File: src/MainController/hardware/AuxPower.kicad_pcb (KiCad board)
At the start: 2 copper layers, 90 x 90 mm, 123 parts, among them J1 MC 1,5/2, J10 MC 1,5/4, J11 S3B-XH-A, J12 S3B-XH-A, J13 S3B-XH-A, J14 S3B-XH-A, J15 S3B-XH-A, J16 B3B-XH-A, J17 B4B-XH-A, J2 MC 1,5/2, J3 MC 1,5/2, J4 MC 1,5/2, J5 MC 1,5/2, J6 MC 1,5/4, J7 MC 1,5/4, J8 MC 1,5/4, J9 MC 1,5/4, Q1 BC846B,235, Q10 AO4421, Q2 BC846B,235, Q3 BC846B,235, Q4 BC846B,235, Q5 BC846B,235, Q6 AO4421, Q7 AO4421, Q8 AO4421, Q9 AO4421, U1 ZXCT1009, U2 ZXCT1009, U3 ZXCT1009, U5 ZXCT1009, U6 PIC18F26K83, U7 PI4IOE5V6416, U8 MCP9701

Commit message: MainController: adjusting voltage dividers
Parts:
- R36: renamed from R37; value 6K2 -> 4K42
- R37: renamed from R38; value 6K2 -> 4K42
- R38: renamed from R39; value 6K2 -> 4K42
- R39: renamed from R40; value 6K2 -> 4K42
- R40: renamed from R41; value 6K2 -> 4K42
- R41: renamed from R29; value 3K -> 5K6
- R57: value 18K -> 39K2
- R58, R59, R60, R61, R62: value 180K -> 137K
- renumbered R30 to R29, R31 to R30, R32 to R31, R33 to R32, R34 to R33, R35 to R34, R36 to R35
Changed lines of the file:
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@@
 		(at 34.8 51 90)
 		(tags "RESC2013X70N")
-		(property "Reference" "R39"
+		(property "Reference" "R38"
 			(at 0 1.6 90)
 			(layer "B.SilkS")
@@
 			)
 		)
-		(property "Value" "6K2"
+		(property "Value" "4K42"
 			(at 2.3 0 0)
 			(layer "B.SilkS")
@@
 			)
 		)
-		(property "Value" "180K"
+		(property "Value" "137K"
 			(at 2.3 0 0)
 			(layer "B.SilkS")
@@
 			)
 		)
-		(property "Value" "180K"
+		(property "Value" "137K"
 			(at 2.3 0 0)
 			(layer "B.SilkS")
@@
 			)
 		)
-		(property "Value" "180K"
+		(property "Value" "137K"
 			(at 2.3 0 0)
 			(layer "B.SilkS")
@@
 		(at 44.4 51 90)
 		(tags "RESC2013X70N")
-		(property "Reference" "R40"
+		(property "Reference" "R39"
 			(at 0 1.6 90)
 			(layer "B.SilkS")
@@
 			)
 		)
-		(property "Value" "6K2"
+		(property "Value" "4K42"
 			(at 2.3 0 0)
 			(layer "B.SilkS")
@@
 		(at 20.5 92 90)
 		(tags "RESC2013X70N")
-		(property "Reference" "R30"
+		(property "Reference" "R29"
 			(at 0 1.6 90)
 			(layer "B.SilkS")
@@
 		(at 38.7 84.15)
 		(tags "RESC2013X70N")
-		(property "Reference" "R36"
+		(property "Reference" "R35"
 			(at 0 1.6 0)
 			(layer "B.SilkS")
@@
 		(at 34.3 84.25 180)
 		(tags "RESC2013X70N")
-		(property "Reference" "R35"
+		(property "Reference" "R34"
 			(at 0 1.6 0)
 			(layer "B.SilkS")
@@
 		(at 54 51 90)
 		(tags "RESC2013X70N")
-		(property "Reference" "R41"
+		(property "Reference" "R40"
 			(at 0 1.6 90)
 			(layer "B.SilkS")
@@
 			)
 		)
-		(property "Value" "6K2"
+		(property "Value" "4K42"
 			(at 2.3 0 0)
 			(layer "B.SilkS")
@@
 		(at 52 92 90)
 		(tags "RESC2013X70N")
-		(property "Reference" "R33"
+		(property "Reference" "R32"
 			(at 0 1.6 90)
 			(layer "B.SilkS")
@@
 		(at 31 92 90)
 		(tags "RESC2013X70N")
-		(property "Reference" "R31"
+		(property "Reference" "R30"
 			(at 0 1.6 90)
 			(layer "B.SilkS")
@@
 		(at 22.8 45 90)
 		(tags "RESC2013X70N")
-		(property "Reference" "R37"
+		(property "Reference" "R36"
 			(at 0 1.6 90)
 			(layer "B.SilkS")
@@
 			)
 		)
-		(property "Value" "6K2"
+		(property "Value" "4K42"
 			(at 2.3 0 0)
 			(layer "B.SilkS")
@@
 			)
 		)
-		(property "Value" "180K"
+		(property "Value" "137K"
 			(at 2.3 0 0)
 			(layer "B.SilkS")
@@
 			)
 		)
-		(property "Value" "18K"
+		(property "Value" "39K2"
 			(at 2.3 0 90)
 			(layer "B.SilkS")
@@
 			)
 		)
-		(property "Value" "180K"
+		(property "Value" "137K"
 			(at 2.3 0 0)
 			(layer "B.SilkS")
@@
 		(at 41.5 92 90)
 		(tags "RESC2013X70N")
-		(property "Reference" "R32"
+		(property "Reference" "R31"
 			(at 0 1.6 90)
 			(layer "B.SilkS")
@@
 		(at 62 84.5 180)
 		(tags "RESC2013X70N")
-		(property "Reference" "R29"
+		(property "Reference" "R41"
 			(at 0 1.6 0)
 			(layer "B.SilkS")
@@
 			)
 		)
-		(property "Value" "3K"
+		(property "Value" "5K6"
 			(at 2.3 0 90)
 			(layer "B.SilkS")
@@
 		(at 62.5 92 90)
 		(tags "RESC2013X70N")
-		(property "Reference" "R34"
+		(property "Reference" "R33"
 			(at 0 1.6 90)
 			(layer "B.SilkS")
@@
 		(at 25.2 51 90)
 		(tags "RESC2013X70N")
-		(property "Reference" "R38"
+		(property "Reference" "R37"
 			(at 0 1.6 90)
 			(layer "B.SilkS")
@@
 			)
 		)
-		(property "Value" "6K2"
+		(property "Value" "4K42"
 			(at 2.3 0 0)
 			(layer "B.SilkS")

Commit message: MainController: Replaced main mosfet
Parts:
- Q10, Q6, Q7, Q8, Q9: value AO4421 -> RS3L110
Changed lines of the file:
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@@
 			)
 		)
-		(property "Value" "AO4421"
+		(property "Value" "RS3L110"
 			(at 0.7 0 0)
 			(layer "B.SilkS")
@@
 			)
 		)
-		(property "Value" "AO4421"
+		(property "Value" "RS3L110"
 			(at 0.7 0 0)
 			(layer "B.SilkS")
@@
 			)
 		)
-		(property "Value" "AO4421"
+		(property "Value" "RS3L110"
 			(at 0.7 0 0)
 			(layer "B.SilkS")
@@
 			)
 		)
-		(property "Value" "AO4421"
+		(property "Value" "RS3L110"
 			(at 0.7 0 0)
 			(layer "B.SilkS")
@@
 			)
 		)
-		(property "Value" "AO4421"
+		(property "Value" "RS3L110"
 			(at 0.7 0 0)
 			(layer "B.SilkS")

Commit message: MainController: Adjusted resistor values for MOSFET drive
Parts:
- R47: renamed from R48; value 10K -> 30K
- R48: renamed from R53; value 18K -> 30K
- R49: renamed from R54; value 18K -> 30K
- R50: renamed from R55; value 18K -> 30K
- R51: renamed from R56; value 18K -> 30K
- R53: renamed from R47; value 10K -> 62K
- R54: renamed from R49; value 10K -> 62K
- R55: renamed from R50; value 10K -> 62K
- R56: renamed from R51; value 10K -> 62K
- R57: renamed from R52; value 10K -> 62K
- renumbered R57 to R52
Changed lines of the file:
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@@
 		(at 70 29.5 180)
 		(tags "RESC2013X70N")
-		(property "Reference" "R51"
+		(property "Reference" "R56"
 			(at 0 1.6 0)
 			(layer "B.SilkS")
@@
 			)
 		)
-		(property "Value" "10K"
+		(property "Value" "62K"
 			(at 2.8 0 0)
 			(layer "B.SilkS")
@@
 		(at 19 29.5 180)
 		(tags "RESC2013X70N")
-		(property "Reference" "R47"
+		(property "Reference" "R53"
 			(at 0 1.6 0)
 			(layer "B.SilkS")
@@
 			)
 		)
-		(property "Value" "10K"
+		(property "Value" "62K"
 			(at 2.7 0 0)
 			(layer "B.SilkS")
@@
 		(at 36 31.7 180)
 		(tags "RESC2013X70N")
-		(property "Reference" "R53"
+		(property "Reference" "R48"
 			(at 0 1.6 0)
 			(layer "B.SilkS")
@@
 			)
 		)
-		(property "Value" "18K"
+		(property "Value" "30K"
 			(at 2.8 0 0)
 			(layer "B.SilkS")
@@
 		(at 70 31.7 180)
 		(tags "RESC2013X70N")
-		(property "Reference" "R55"
+		(property "Reference" "R50"
 			(at 0 1.6 0)
 			(layer "B.SilkS")
@@
 			)
 		)
-		(property "Value" "18K"
+		(property "Value" "30K"
 			(at 2.8 0 0)
 			(layer "B.SilkS")
@@
 		(at 87 31.7 180)
 		(tags "RESC2013X70N")
-		(property "Reference" "R56"
+		(property "Reference" "R51"
 			(at 0 1.6 0)
 			(layer "B.SilkS")
@@
 			)
 		)
-		(property "Value" "18K"
+		(property "Value" "30K"
 			(at 2.8 0 0)
 			(layer "B.SilkS")
@@
 		(at 36 29.5 180)
 		(tags "RESC2013X70N")
-		(property "Reference" "R49"
+		(property "Reference" "R54"
 			(at 0 1.6 0)
 			(layer "B.SilkS")
@@
 			)
 		)
-		(property "Value" "10K"
+		(property "Value" "62K"
 			(at 2.8 0 0)
 			(layer "B.SilkS")
@@
 		(at 53 31.7 180)
 		(tags "RESC2013X70N")
-		(property "Reference" "R54"
+		(property "Reference" "R49"
 			(at 0 1.6 0)
 			(layer "B.SilkS")
@@
 			)
 		)
-		(property "Value" "18K"
+		(property "Value" "30K"
 			(at 2.8 0 0)
 			(layer "B.SilkS")
@@
 		(at 19 31.7 180)
 		(tags "RESC2013X70N")
-		(property "Reference" "R48"
+		(property "Reference" "R47"
 			(at 0 1.6 0)
 			(layer "B.SilkS")
@@
 			)
 		)
-		(property "Value" "10K"
+		(property "Value" "30K"
 			(at 2.7 0 0)
 			(layer "B.SilkS")
@@
 		(at 53 29.5 180)
 		(tags "RESC2013X70N")
-		(property "Reference" "R50"
+		(property "Reference" "R55"
 			(at 0 1.6 0)
 			(layer "B.SilkS")
@@
 			)
 		)
-		(property "Value" "10K"
+		(property "Value" "62K"
 			(at 2.8 0 0)
 			(layer "B.SilkS")
@@
 		(at 62 82.1 180)
 		(tags "RESC2013X70N")
-		(property "Reference" "R57"
+		(property "Reference" "R52"
 			(at 0 1.6 0)
 			(layer "B.SilkS")
@@
 		(at 87 29.5 180)
 		(tags "RESC2013X70N")
-		(property "Reference" "R52"
+		(property "Reference" "R57"
 			(at 0 1.6 0)
 			(layer "B.SilkS")
@@
 			)
 		)
-		(property "Value" "10K"
+		(property "Value" "62K"
 			(at 2.8 0 0)
 			(layer "B.SilkS")

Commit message: MainController: Reducing internal LED brightness
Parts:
- R22, R23, R24, R25, R26, R27: value 1K -> 3K3
- R28: renamed from R21; value 1K -> 3K3
- renumbered R28 to R21
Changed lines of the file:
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@@
 		(at 23 92 90)
 		(tags "RESC2013X70N")
-		(property "Reference" "R21"
+		(property "Reference" "R28"
 			(at 0 1.6 90)
 			(layer "B.SilkS")
@@
 			)
 		)
-		(property "Value" "1K"
+		(property "Value" "3K3"
 			(at 2.3 0 0)
 			(layer "B.SilkS")
@@
 		(at 40.5 66.5 180)
 		(tags "RESC2013X70N")
-		(property "Reference" "R28"
+		(property "Reference" "R21"
 			(at 0 1.6 0)
 			(layer "B.SilkS")
@@
 			)
 		)
-		(property "Value" "1K"
+		(property "Value" "3K3"
 			(at 2.3 0 0)
 			(layer "B.SilkS")
@@
 			)
 		)
-		(property "Value" "1K"
+		(property "Value" "3K3"
 			(at 2.3 0 0)
 			(layer "B.SilkS")
@@
 			)
 		)
-		(property "Value" "1K"
+		(property "Value" "3K3"
 			(at 2.3 0 0)
 			(layer "B.SilkS")
@@
 			)
 		)
-		(property "Value" "1K"
+		(property "Value" "3K3"
 			(at 0 1.7 0)
 			(layer "B.SilkS")
@@
 			)
 		)
-		(property "Value" "1K"
+		(property "Value" "3K3"
 			(at -2.35 -0.05 0)
 			(layer "B.SilkS")
@@
 			)
 		)
-		(property "Value" "1K"
+		(property "Value" "3K3"
 			(at 2.3 0 0)
 			(layer "B.SilkS")

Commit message: MainController: Reducing brightness for output LEDs
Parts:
- R17: renamed from R16; value 1K -> 3K3
- R18: renamed from R17; value 1K -> 3K3
- R19: renamed from R18; value 1K -> 3K3
- R20: renamed from R19; value 1K -> 3K3
- R21: renamed from R20; value 1K -> 3K3
- renumbered R21 to R16
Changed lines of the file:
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@@
 		(at 48.1 65 -90)
 		(tags "RESC2013X70N")
-		(property "Reference" "R20"
+		(property "Reference" "R21"
 			(at 0 1.6 90)
 			(layer "B.SilkS")
@@
 			)
 		)
-		(property "Value" "1K"
+		(property "Value" "3K3"
 			(at -2.3 0 0)
 			(layer "B.SilkS")
@@
 		(at 42.6 59.7 -90)
 		(tags "RESC2013X70N")
-		(property "Reference" "R16"
+		(property "Reference" "R17"
 			(at 0 1.6 90)
 			(layer "B.SilkS")
@@
 			)
 		)
-		(property "Value" "1K"
+		(property "Value" "3K3"
 			(at -2.3 0.3 0)
 			(layer "B.SilkS")
@@
 		(at 49.2 59.7 -90)
 		(tags "RESC2013X70N")
-		(property "Reference" "R19"
+		(property "Reference" "R20"
 			(at 0 1.6 90)
 			(layer "B.SilkS")
@@
 			)
 		)
-		(property "Value" "1K"
+		(property "Value" "3K3"
 			(at -2.3 -0.25 0)
 			(layer "B.SilkS")
@@
 		(at 40.5 66.5 180)
 		(tags "RESC2013X70N")
-		(property "Reference" "R21"
+		(property "Reference" "R16"
 			(at 0 1.6 0)
 			(layer "B.SilkS")
@@
 		(at 44.8 59.7 -90)
 		(tags "RESC2013X70N")
-		(property "Reference" "R17"
+		(property "Reference" "R18"
 			(at 0 1.6 90)
 			(layer "B.SilkS")
@@
 			)
 		)
-		(property "Value" "1K"
+		(property "Value" "3K3"
 			(at -2.3 0.1 0)
 			(layer "B.SilkS")
@@
 		(at 47 59.7 -90)
 		(tags "RESC2013X70N")
-		(property "Reference" "R18"
+		(property "Reference" "R19"
 			(at 0 1.6 90)
 			(layer "B.SilkS")
@@
 			)
 		)
-		(property "Value" "1K"
+		(property "Value" "3K3"
 			(at -2.3 -0.1 0)
 			(layer "B.SilkS")
@@
 		)
 		(property "Value" "3K3"
-			(at -2.35 -0.05 0)
+			(at -2.8 0.05 0)
 			(layer "B.SilkS")
 			(effects

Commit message: MainController: updated refdes
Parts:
- renumbered D2 to D3, U5 to U4
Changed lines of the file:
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@@
 		(at 52.3 27.1 180)
 		(descr "Onsemi SS24FL")
-		(property "Reference" "D2"
+		(property "Reference" "D3"
 			(at 0.1 0 0)
 			(layer "B.SilkS")
@@
 		(at 57.4 38.9 180)
 		(tags "SOT95P240X110-3N")
-		(property "Reference" "U5"
+		(property "Reference" "U4"
 			(at 0 2.2 0)
 			(layer "B.SilkS")

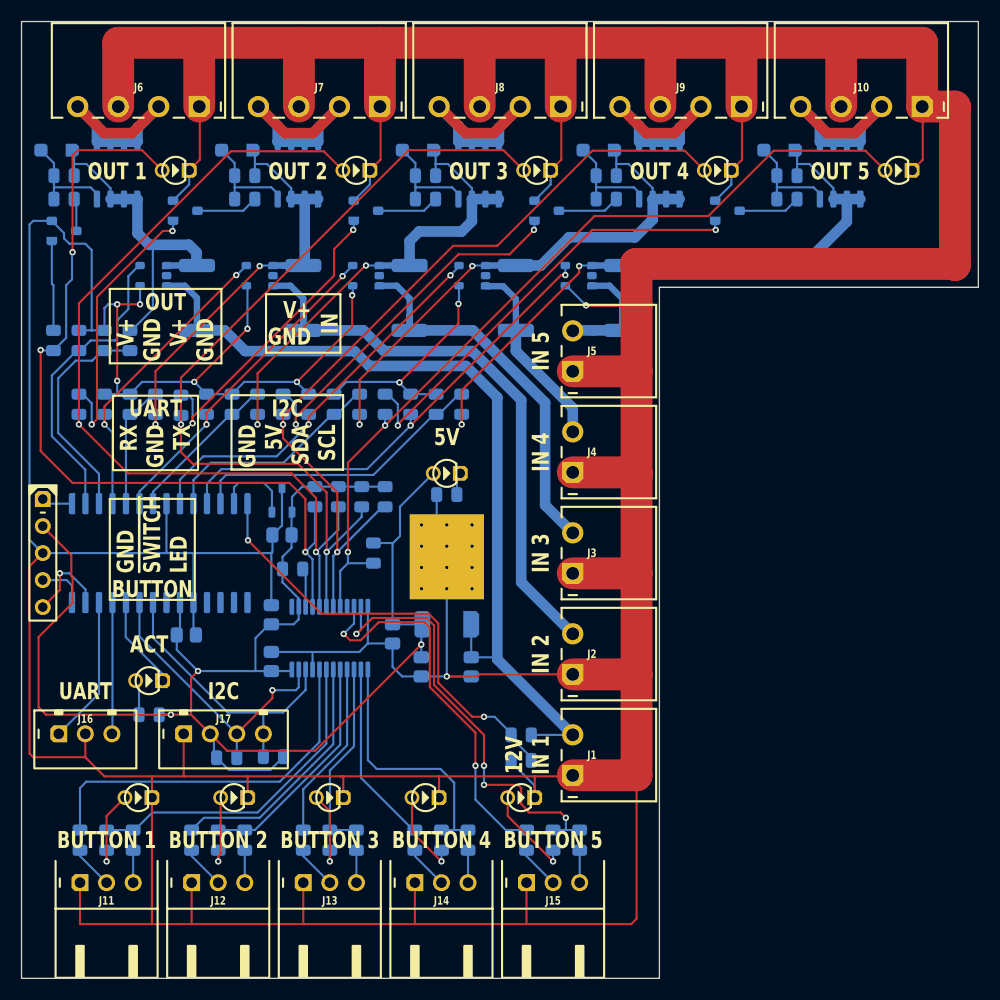
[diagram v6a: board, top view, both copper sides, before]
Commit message: MainController: Moving voltage for PIC after shunt resistor
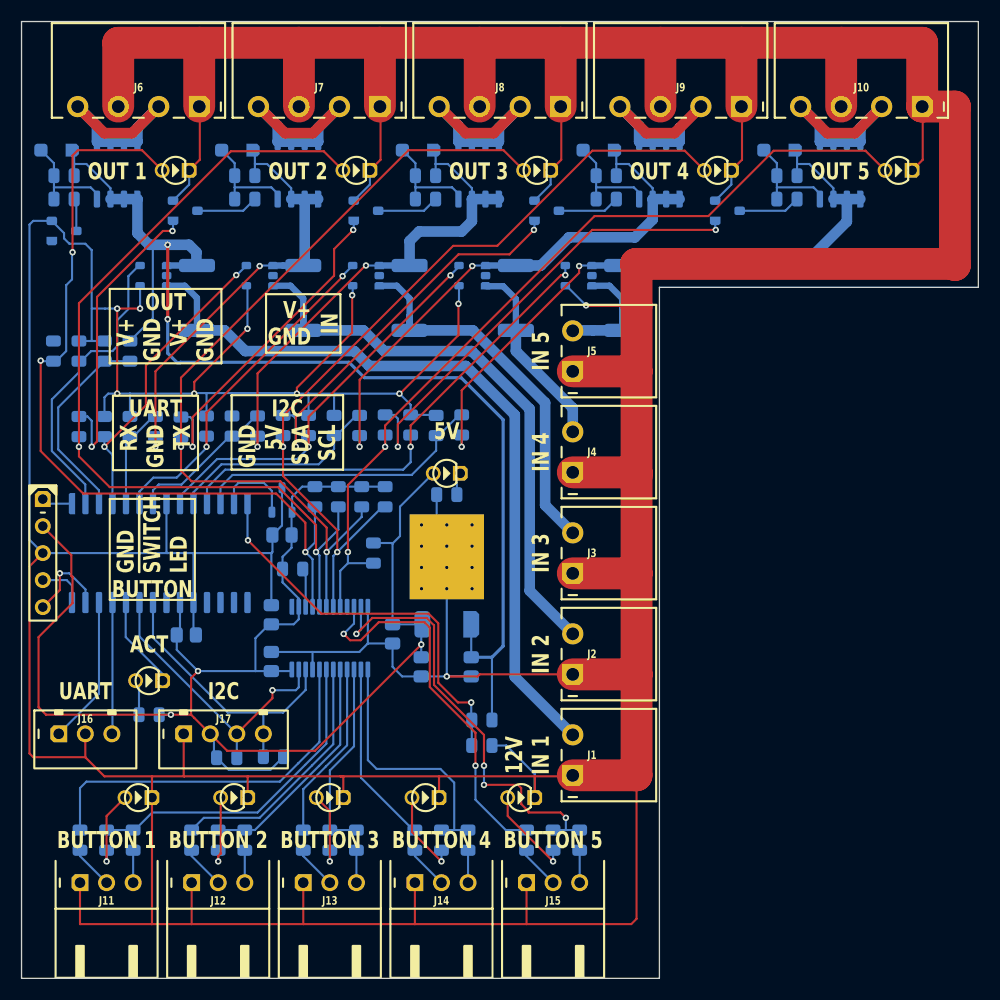
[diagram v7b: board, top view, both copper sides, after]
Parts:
- moved R41 3.96 mm to (58.3, 83.1), turned to 0 degrees
- moved R52 3.96 mm to (58.3, 80.7)
- moved R12 2.10 mm to (22.8, 53.1)
- moved R37 2.10 mm to (25.2, 53.1)
- moved R43 2.10 mm to (20.4, 53.1)
- moved R59 2.10 mm to (27.6, 53.1)
- moved R13 2.05 mm to (32.4, 53.0)
- moved R38 2.05 mm to (34.8, 53.0)
- moved R44 2.05 mm to (30.0, 53.1)
- moved R60 2.05 mm to (37.2, 53.0)
- moved R14 2.00 mm to (42.0, 53.0)
- moved R39 2.00 mm to (44.4, 53.0)
- moved R40 2.00 mm to (54.0, 53.0)
- moved R45 2.00 mm to (39.6, 53.0)
- moved R61 2.00 mm to (46.8, 53.0)
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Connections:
- C7 pad 2: INPUT1 -> INPUT1'
- R52 pad 1: INPUT1 -> INPUT1'
- VR1 pad 1: INPUT1 -> INPUT1'
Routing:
- net INPUT1': track 32.4 -> 115.8 mm, vias 0 -> 2
- net GND: track 759.7 -> 776.8 mm
- net INPUT1: track 81.4 -> 71.9 mm
- net BASE1: track 8.46 -> 0.00 mm
- net ADC_VOLTAGE_IN: track 41.7 -> 38.1 mm
- net BASE4: track 34.5 -> 37.5 mm
- net BASE5: track 41.8 -> 44.7 mm
- net BASE2: track 26.0 -> 28.8 mm
- net BASE3: track 28.8 -> 31.5 mm
- net INPUT4': track 50.9 -> 53.4 mm
- net INPUT3': track 45.4 -> 47.7 mm
- net INPUT5': track 59.8 -> 62.0 mm
- net ADC_VOLTAGE2: track 10.7 -> 8.61 mm
- net INPUT2': track 40.5 -> 42.5 mm
- net ADC_VOLTAGE1: track 21.0 -> 19.2 mm
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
